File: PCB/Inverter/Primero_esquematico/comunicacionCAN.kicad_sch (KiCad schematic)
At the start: 12 parts, among them J10 430450414, J11 430450414, U27 ISO1042DWR, U28 ISO1042DWR

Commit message: Un par de cosas q corregi del ERC pero sigue mal
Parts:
- U27, U28: footprint Snapeda:DW0016B_HV -> DW0016B_N
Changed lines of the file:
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@@
 	)
 	(hierarchical_label "TX2_can"
-		(shape input)
+		(shape bidirectional)
 		(at 83.82 127 180)
 		(effects
@@
 	)
 	(hierarchical_label "RX2_can"
-		(shape input)
+		(shape bidirectional)
 		(at 83.82 132.08 180)
 		(effects
@@
 	)
 	(hierarchical_label "TX1_can"
-		(shape input)
+		(shape bidirectional)
 		(at 82.55 63.5 180)
 		(effects
@@
 	)
 	(hierarchical_label "RX1_can"
-		(shape input)
+		(shape bidirectional)
 		(at 82.55 68.58 180)
 		(effects
@@
 			)
 		)
-		(property "Datasheet" "https://assets.nexperia.com/documents/data-sheet/PESD2CANFD24LT-Q.pdf"
+		(property "Datasheet" "https://www.littelfuse.com/~/media/electronics/datasheets/tvs_diode_arrays/littelfuse_tvs_diode_array_sm712_datasheet.pdf.pdf"
 			(at 134.62 144.78 0)
 			(hide yes)
@@
 			)
 		)
-		(property "Description" "TVS DIODE 24VWM 41VC TO236AB"
+		(property "Description" "7V/12V, 600W Asymmetrical TVS Diode Array, SOT-23"
 			(at 138.43 144.78 0)
 			(hide yes)
@@
 			)
 		)
-		(property "Footprint" "Snapeda:DW0016B_HV"
+		(property "Footprint" "DW0016B_N"
 			(at 102.87 48.26 0)
 			(hide yes)
@@
 			)
 		)
-		(property "Description" "-- valores mixtos --"
+		(property "Description" "Resistor, small symbol"
 			(at 125.73 68.58 0)
 			(hide yes)
@@
 			)
 		)
-		(property "Description" "-- valores mixtos --"
+		(property "Description" "Resistor, small symbol"
 			(at 127 132.08 0)
 			(hide yes)
@@
 			)
 		)
-		(property "Footprint" "Snapeda:DW0016B_HV"
+		(property "Footprint" "DW0016B_N"
 			(at 104.14 111.76 0)
 			(hide yes)
@@
 			)
 		)
-		(property "Datasheet" "https://assets.nexperia.com/documents/data-sheet/PESD2CANFD24LT-Q.pdf"
+		(property "Datasheet" "https://www.littelfuse.com/~/media/electronics/datasheets/tvs_diode_arrays/littelfuse_tvs_diode_array_sm712_datasheet.pdf.pdf"
 			(at 133.35 81.28 0)
 			(hide yes)
@@
 			)
 		)
-		(property "Description" "TVS DIODE 24VWM 41VC TO236AB"
+		(property "Description" "7V/12V, 600W Asymmetrical TVS Diode Array, SOT-23"
 			(at 137.16 81.28 0)
 			(hide yes)

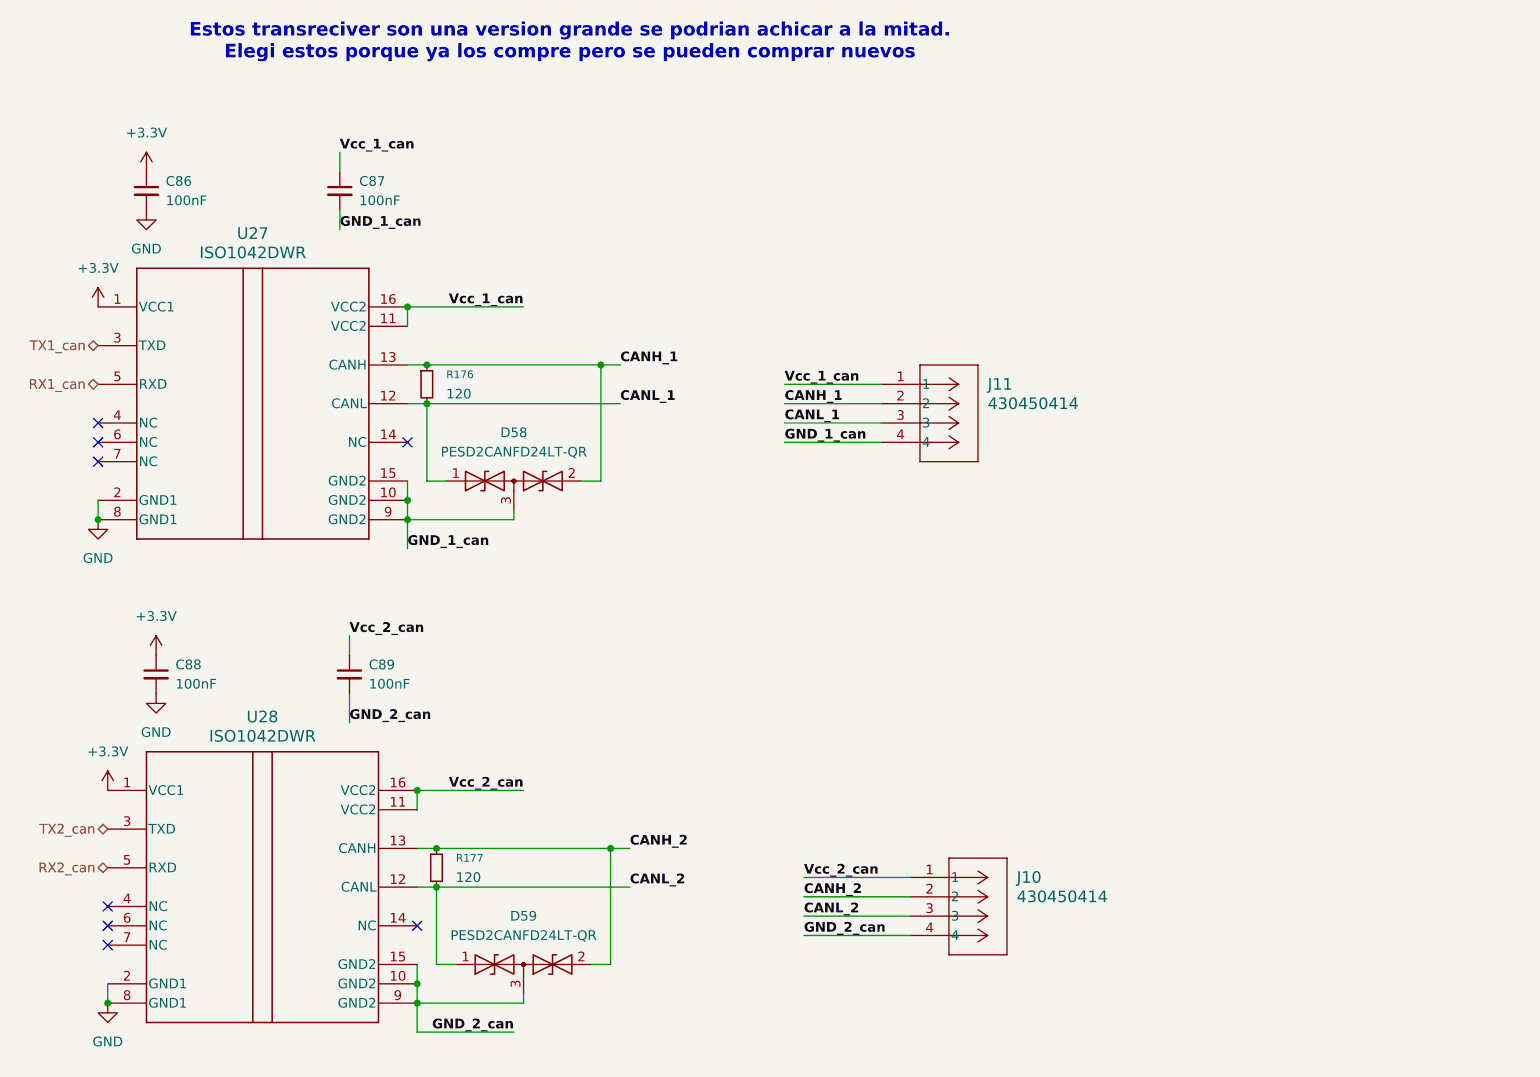
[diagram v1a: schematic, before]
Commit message: Esquematico Listo
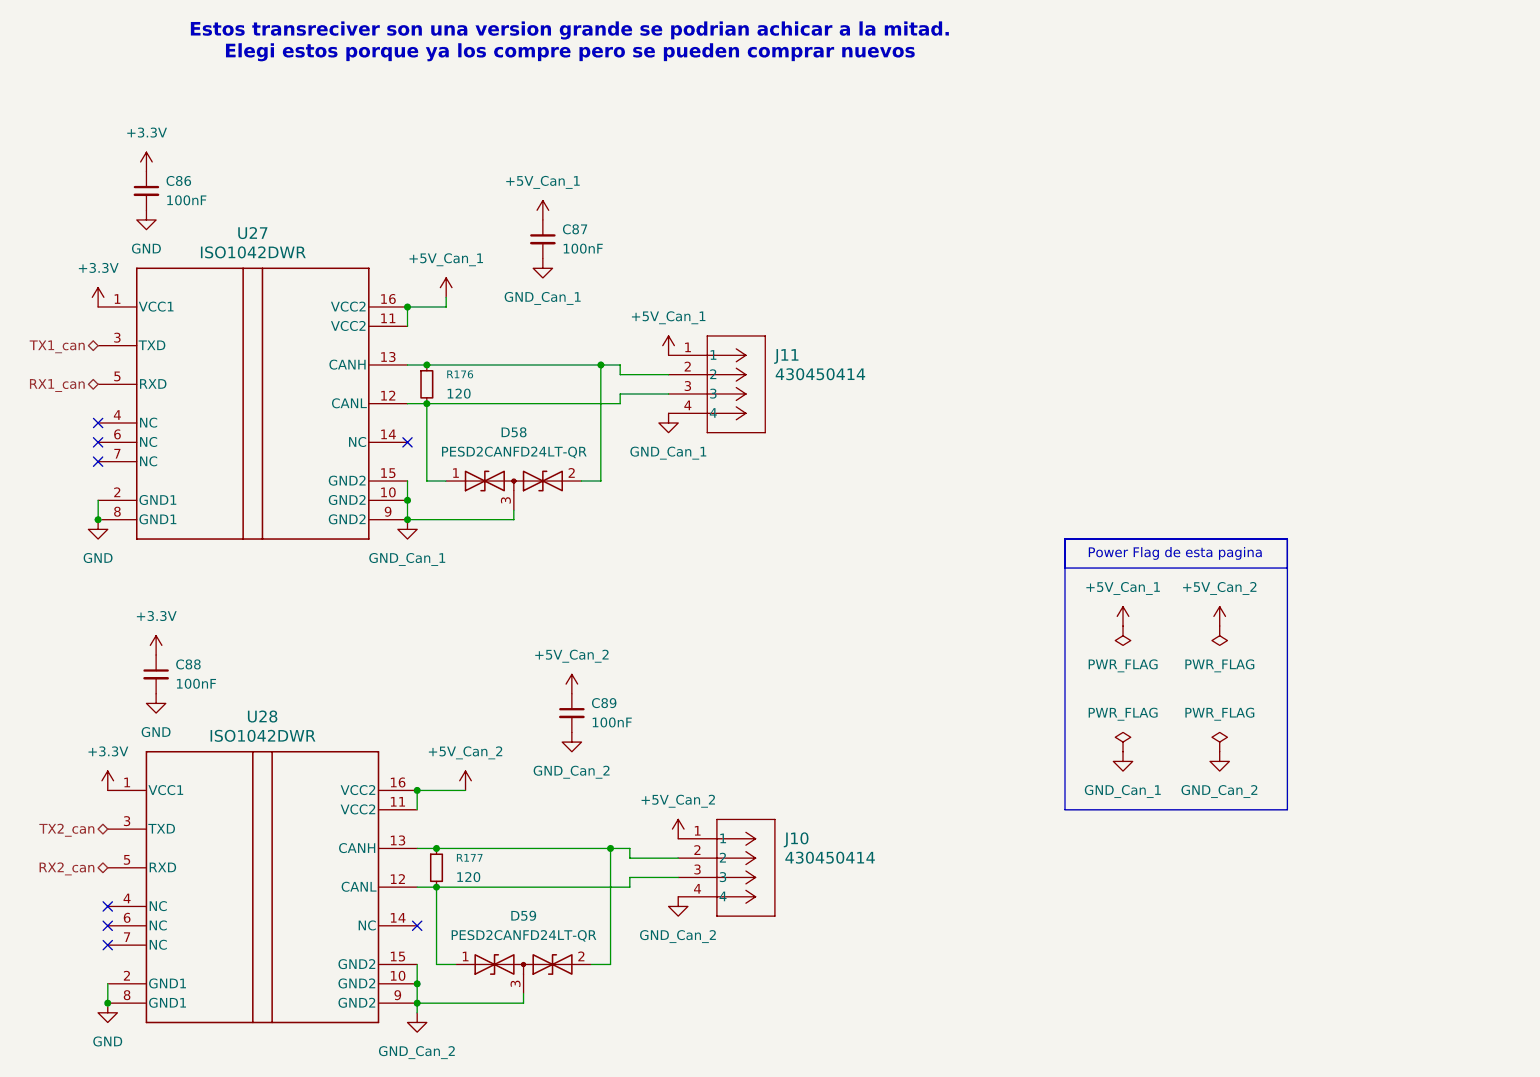
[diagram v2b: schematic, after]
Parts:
- J10, J11: footprint CONN_SD-43045-005_04_MOL -> Snapeda:CONN_SD-43045-005_04_MOL
- U27, U28: footprint DW0016B_N -> Snapeda:DW0016B_HV
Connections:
- net CANH_1: no longer names the net of D58.2 (A2), J11.2, R176.1, U27.13 (CANH)
- net CANH_2: no longer names the net of D59.2 (A2), J10.2, R177.1, U28.13 (CANH)
- net CANL_1: no longer names the net of D58.1 (A1), J11.3, R176.2, U27.12 (CANL)
- net CANL_2: no longer names the net of D59.1 (A1), J10.3, R177.2, U28.12 (CANL)
- net GND_1_can renamed GND_Can_1
- net GND_2_can renamed GND_Can_2
- net Vcc_1_can renamed +5V_Can_1
- net Vcc_2_can renamed +5V_Can_2
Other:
- note added: "Power Flag de esta pagina"
- moved on the sheet: C87, C89, J10, J11

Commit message: correcciones
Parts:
- removed J10, J11: 430450414, Snapeda:CONN_SD-43045-005_04_MOL, symbol Snapeda:430450414
- added J2, J3: 430450402, Snapeda:CONN_SD-43045-001_04_MOL, symbol Snapeda:430450402
- renumbered C86 to C131, C88 to C132, C89 to C133, C87 to C134, D58 to D81, D59 to D82, R176 to R190, R177 to R191, U27 to U32, U28 to U33
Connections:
- net +5V_Can_1: now also J2.1
- net +5V_Can_2: now also J3.1
- net GND_Can_1: now also J2.2
- net GND_Can_2: now also J3.2
- net at R190.1, U32.13 (CANH): now also D81.1 (A1), J2.3; no longer D81.2 (A2)
- net at R190.2, U32.12 (CANL): now also D81.2 (A2), J2.4; no longer D81.1 (A1)
- net at R191.2, U33.12 (CANL): now also D82.2 (A2), J3.4; no longer D82.1 (A1)
- net at R191.1, U33.13 (CANH): now also D82.1 (A1), J3.3; no longer D82.2 (A2)
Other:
- moved on the sheet: C133, R190, R191

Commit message: Algunos cambios
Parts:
- removed J2, J3: 430450402, Snapeda:CONN_SD-43045-001_04_MOL, symbol Snapeda:430450402
- added J6, J7: 347920040, Snapeda:CONN04_34792_MOL, symbol Snapeda:347920040
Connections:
- net +5V_Can_1: now also J7.4
- net +5V_Can_2: now also J6.4
- net GND_Can_1: now also J7.3
- net GND_Can_2: now also J6.3
- net at D82.1 (A1), R191.1, U33.13 (CANH): now also J6.2
- net at D82.2 (A2), R191.2, U33.12 (CANL): now also J6.1
- net at D81.2 (A2), R190.2, U32.12 (CANL): now also J7.1
- net at D81.1 (A1), R190.1, U32.13 (CANH): now also J7.2
- net +3.3V renamed +3.3_digital
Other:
- note added: "ISO 11898-2 -> Esta norma especifica la impedancia caracteristica"
- note added: "La utilizacion de la resitencia de 120 Ohms es para adaptar la linea esto sirve para velocidades de conmutacion rapidas y es valida cuando el cable que se utiliza tiene una impedancia caracteristica de 120 Ohms. En caso de que no se cumpla eso la linea estara desadaptada y la funcion de la resistencia no tendra mucho sentido. Si se utiliza un CAN paracomunicar muchos nodos tampoco tiene sentido l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"
- note added: "Uso de la resistencia de 120 Ohms"

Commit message: Corregi cosas de la placa
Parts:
- renumbered C131 to C151, C132 to C152, C133 to C153, C134 to C154, D81 to D80, D82 to D81, J7 to J3, J6 to J4, U32 to U31, U33 to U32
